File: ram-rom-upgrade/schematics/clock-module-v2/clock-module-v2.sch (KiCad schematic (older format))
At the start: 24 parts, among them SW1 SW_Push, SW2 SW_SPDT, U1 LM555, U4 74LS04, U5 74LS08, U6 74LS32

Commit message: minor tweaks
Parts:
- RV1: symbol clock-module-with-prog-halt-rescue:POT-8bit-computer-rescue-8bit-computer-rescue -> clock-module-v2-rescue:POT-8bit-computer-rescue-8bit-computer-rescue-clock-module-with-prog-halt-rescue
- SW1: symbol clock-module-with-prog-halt-rescue:SW_Push-8bit-computer-rescue-8bit-computer-rescue -> clock-module-v2-rescue:SW_Push-8bit-computer-rescue-8bit-computer-rescue-clock-module-with-prog-halt-rescue
- SW2: symbol clock-module-with-prog-halt-rescue:SW_SPDT-8bit-computer-rescue-8bit-computer-rescue -> clock-module-v2-rescue:SW_SPDT-8bit-computer-rescue-8bit-computer-rescue-clock-module-with-prog-halt-rescue
- U1: symbol clock-module-with-prog-halt-rescue:LM555-8bit-computer-rescue-8bit-computer-rescue -> clock-module-v2-rescue:LM555-8bit-computer-rescue-8bit-computer-rescue-clock-module-with-prog-halt-rescue
- U4: symbol clock-module-with-prog-halt-rescue:74LS04-8bit-computer-rescue-8bit-computer-rescue -> clock-module-v2-rescue:74LS04-8bit-computer-rescue-8bit-computer-rescue-clock-module-with-prog-halt-rescue
- U5: symbol clock-module-with-prog-halt-rescue:74LS08-8bit-computer-rescue-8bit-computer-rescue -> clock-module-v2-rescue:74LS08-8bit-computer-rescue-8bit-computer-rescue-clock-module-with-prog-halt-rescue
- U6: symbol clock-module-with-prog-halt-rescue:74LS32-8bit-computer-rescue-8bit-computer-rescue -> clock-module-v2-rescue:74LS32-8bit-computer-rescue-8bit-computer-rescue-clock-module-with-prog-halt-rescue
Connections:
- net CLK: now also U4.9; no longer U4.13
- net HLT: now also U4.11; no longer U4.9
- net PROG: now also U4.13; no longer U4.11
- net ~CLK: now also U4.8; no longer U4.12
- net at U5.12: now also U4.10; no longer U4.8
- net at U5.13: now also U4.12; no longer U4.10
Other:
- moved on the sheet: U4D, U4E, U4F
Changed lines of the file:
@@
 $EndDescr
 $Comp
-L clock-module-with-prog-halt-rescue:LM555-8bit-computer-rescue-8bit-computer-rescue U1
+L clock-module-v2-rescue:LM555-8bit-computer-rescue-8bit-computer-rescue-clock-module-with-prog-halt-rescue U1
 U 1 1 5B52B53B
 P 2000 2100
@@
 $EndComp
 $Comp
-L clock-module-with-prog-halt-rescue:POT-8bit-computer-rescue-8bit-computer-rescue RV1
+L clock-module-v2-rescue:POT-8bit-computer-rescue-8bit-computer-rescue-clock-module-with-prog-halt-rescue RV1
 U 1 1 5B52B6D7
 P 3150 2200
@@
 $EndComp
 $Comp
-L clock-module-with-prog-halt-rescue:74LS04-8bit-computer-rescue-8bit-computer-rescue U4
+L clock-module-v2-rescue:74LS04-8bit-computer-rescue-8bit-computer-rescue-clock-module-with-prog-halt-rescue U4
 U 1 1 5B52B95A
 P 3000 4900
@@
 $EndComp
 $Comp
-L clock-module-with-prog-halt-rescue:74LS08-8bit-computer-rescue-8bit-computer-rescue U5
+L clock-module-v2-rescue:74LS08-8bit-computer-rescue-8bit-computer-rescue-clock-module-with-prog-halt-rescue U5
 U 1 1 5B52B9AD
 P 4200 4200
@@
 $EndComp
 $Comp
-L clock-module-with-prog-halt-rescue:74LS32-8bit-computer-rescue-8bit-computer-rescue U6
+L clock-module-v2-rescue:74LS32-8bit-computer-rescue-8bit-computer-rescue-clock-module-with-prog-halt-rescue U6
 U 1 1 5B52B9E8
 P 5600 4600
@@
 $EndComp
 $Comp
-L clock-module-with-prog-halt-rescue:SW_SPDT-8bit-computer-rescue-8bit-computer-rescue SW2
+L clock-module-v2-rescue:SW_SPDT-8bit-computer-rescue-8bit-computer-rescue-clock-module-with-prog-halt-rescue SW2
 U 1 1 5B52BA7F
 P 6850 2200
@@
 $EndComp
 $Comp
-L clock-module-with-prog-halt-rescue:SW_Push-8bit-computer-rescue-8bit-computer-rescue SW1
+L clock-module-v2-rescue:SW_Push-8bit-computer-rescue-8bit-computer-rescue-clock-module-with-prog-halt-rescue SW1
 U 1 1 5B52BB68
 P 3950 1900
@@
 NoConn ~ 8450 2100
 $Comp
-L clock-module-with-prog-halt-rescue:74LS08-8bit-computer-rescue-8bit-computer-rescue U5
+L clock-module-v2-rescue:74LS08-8bit-computer-rescue-8bit-computer-rescue-clock-module-with-prog-halt-rescue U5
 U 2 1 5B52E719
 P 4200 5000
@@
 $EndComp
 $Comp
-L clock-module-with-prog-halt-rescue:74LS08-8bit-computer-rescue-8bit-computer-rescue U5
+L clock-module-v2-rescue:74LS08-8bit-computer-rescue-8bit-computer-rescue-clock-module-with-prog-halt-rescue U5
 U 3 1 5B52E764
 P 7000 4700
@@
 $EndComp
 $Comp
-L clock-module-with-prog-halt-rescue:74LS04-8bit-computer-rescue-8bit-computer-rescue U4
+L clock-module-v2-rescue:74LS04-8bit-computer-rescue-8bit-computer-rescue-clock-module-with-prog-halt-rescue U4
 U 4 1 5B52E7BF
-P 3000 5800
-F 0 "U4" H 3195 5915 50  0000 C CNN
-F 1 "74LS04" H 3190 5675 50  0000 C CNN
-F 2 "Package_DIP:DIP-14_W7.62mm" H 3000 5800 50  0001 C CNN
-F 3 "" H 3000 5800 50  0001 C CNN
-	4    3000 5800
-	1    0    0    -1
-$EndComp
-$Comp
-L clock-module-with-prog-halt-rescue:74LS04-8bit-computer-rescue-8bit-computer-rescue U4
-U 6 1 5B52E82B
 P 8800 4250
 F 0 "U4" H 8995 4365 50  0000 C CNN
@@
 F 2 "Package_DIP:DIP-14_W7.62mm" H 8800 4250 50  0001 C CNN
 F 3 "" H 8800 4250 50  0001 C CNN
-	6    8800 4250
+	4    8800 4250
+	1    0    0    -1
+$EndComp
+$Comp
+L clock-module-v2-rescue:74LS04-8bit-computer-rescue-8bit-computer-rescue-clock-module-with-prog-halt-rescue U4
+U 6 1 5B52E82B
+P 2250 6000
+F 0 "U4" H 2445 6115 50  0000 C CNN
+F 1 "74LS04" H 2440 5875 50  0000 C CNN
+F 2 "Package_DIP:DIP-14_W7.62mm" H 2250 6000 50  0001 C CNN
+F 3 "" H 2250 6000 50  0001 C CNN
+	6    2250 6000
 	1    0    0    -1
 $EndComp
@@
 	9900 1750 9900 1850
 $Comp
-L clock-module-with-prog-halt-rescue:74LS04-8bit-computer-rescue-8bit-computer-rescue U4
+L clock-module-v2-rescue:74LS04-8bit-computer-rescue-8bit-computer-rescue-clock-module-with-prog-halt-rescue U4
 U 2 1 5B5304B0
 P 1700 6650
@@
 $EndComp
 $Comp
-L clock-module-with-prog-halt-rescue:74LS04-8bit-computer-rescue-8bit-computer-rescue U4
+L clock-module-v2-rescue:74LS04-8bit-computer-rescue-8bit-computer-rescue-clock-module-with-prog-halt-rescue U4
 U 3 1 5B5304FB
 P 1700 7050
@@
 $EndComp
 $Comp
-L clock-module-with-prog-halt-rescue:74LS04-8bit-computer-rescue-8bit-computer-rescue U4
+L clock-module-v2-rescue:74LS04-8bit-computer-rescue-8bit-computer-rescue-clock-module-with-prog-halt-rescue U4
 U 5 1 5B53108F
-P 2250 6000
-F 0 "U4" H 2445 6115 50  0000 C CNN
-F 1 "74LS04" H 2440 5875 50  0000 C CNN
-F 2 "Package_DIP:DIP-14_W7.62mm" H 2250 6000 50  0001 C CNN
-F 3 "" H 2250 6000 50  0001 C CNN
-	5    2250 6000
-	1    0    0    -1
-$EndComp
-$Comp
-L clock-module-with-prog-halt-rescue:74LS08-8bit-computer-rescue-8bit-computer-rescue U5
+P 3000 5800
+F 0 "U4" H 3195 5915 50  0000 C CNN
+F 1 "74LS04" H 3190 5675 50  0000 C CNN
+F 2 "Package_DIP:DIP-14_W7.62mm" H 3000 5800 50  0001 C CNN
+F 3 "" H 3000 5800 50  0001 C CNN
+	5    3000 5800
+	1    0    0    -1
+$EndComp
+$Comp
+L clock-module-v2-rescue:74LS08-8bit-computer-rescue-8bit-computer-rescue-clock-module-with-prog-halt-rescue U5
 U 4 1 5B53125C
 P 4250 5900
@@
 $EndComp
 $Comp
-L clock-module-with-prog-halt-rescue:74LS32-8bit-computer-rescue-8bit-computer-rescue U6
+L clock-module-v2-rescue:74LS32-8bit-computer-rescue-8bit-computer-rescue-clock-module-with-prog-halt-rescue U6
 U 2 1 5B5312F6
 P 3000 7400
@@
 $EndComp
 $Comp
-L clock-module-with-prog-halt-rescue:74LS32-8bit-computer-rescue-8bit-computer-rescue U6
+L clock-module-v2-rescue:74LS32-8bit-computer-rescue-8bit-computer-rescue-clock-module-with-prog-halt-rescue U6
 U 3 1 5B5313CF
 P 4350 6800
@@
 PROG
 $Comp
-L clock-module-with-prog-halt-rescue:74LS32-8bit-computer-rescue-8bit-computer-rescue U6
+L clock-module-v2-rescue:74LS32-8bit-computer-rescue-8bit-computer-rescue-clock-module-with-prog-halt-rescue U6
 U 4 1 5B531491
 P 4350 7400

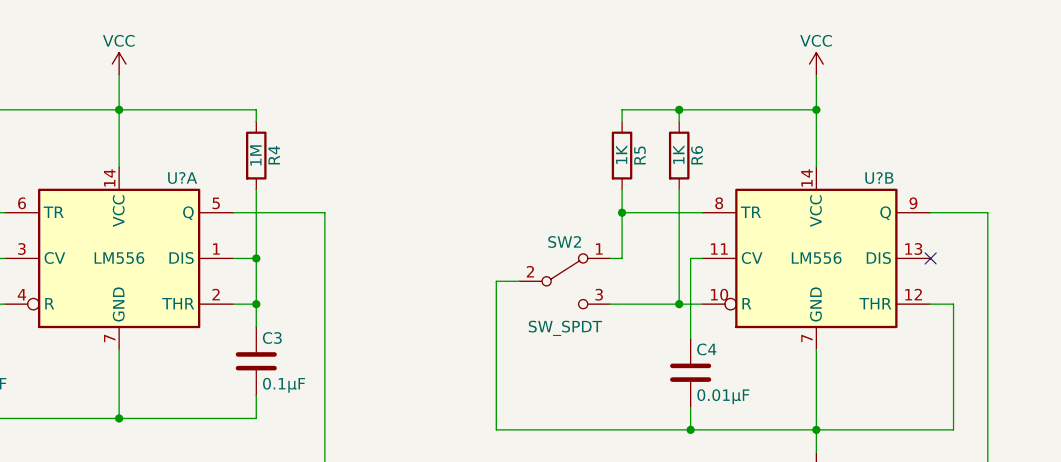
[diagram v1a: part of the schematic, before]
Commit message: added annotations
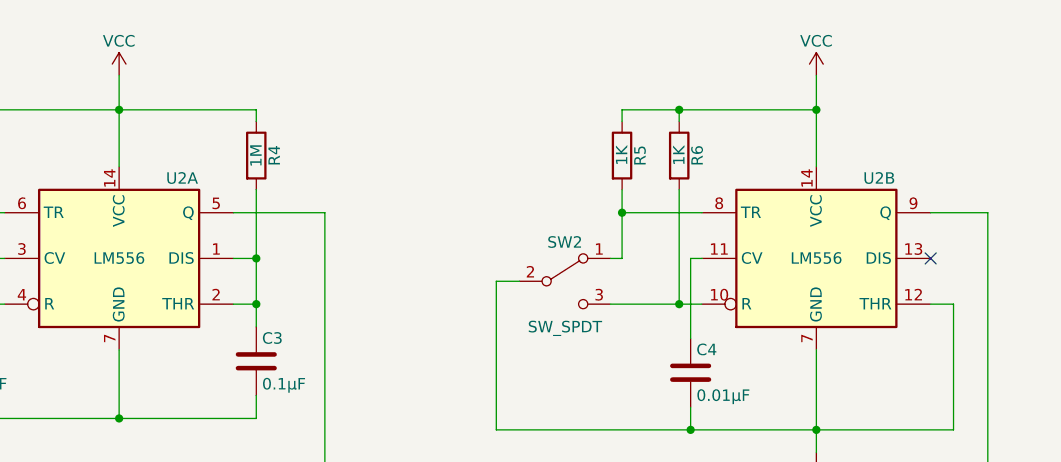
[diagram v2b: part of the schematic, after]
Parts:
- gave numbers to parts that had none: 1
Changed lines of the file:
@@
 	2700 6000 3650 6000
 $Comp
-L Timer:LM556 U?
+L Timer:LM556 U2
 U 1 1 607D2826
 P 4900 2100
-F 0 "U?" H 5175 2450 50  0000 C CNN
+F 0 "U2" H 5175 2450 50  0000 C CNN
 F 1 "LM556" H 4900 2100 50  0000 C CNN
 F 2 "" H 4900 2100 50  0001 C CNN
@@
 $EndComp
 $Comp
-L Timer:LM556 U?
+L Timer:LM556 U2
 U 2 1 607D78F1
 P 7950 2100
-F 0 "U?" H 8225 2450 50  0000 C CNN
+F 0 "U2" H 8225 2450 50  0000 C CNN
 F 1 "LM556" H 7950 2100 50  0000 C CNN
 F 2 "" H 7950 2100 50  0001 C CNN

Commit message: candidate final schematic designs
Also started to consolidate custom symbols from all projects
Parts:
- RV1: symbol clock-module-v2-rescue:POT-8bit-computer-rescue-8bit-computer-rescue-clock-module-with-prog-halt-rescue -> Device:R_POT
- SW1: symbol clock-module-v2-rescue:SW_Push-8bit-computer-rescue-8bit-computer-rescue-clock-module-with-prog-halt-rescue -> Switch:SW_Push
- SW2: symbol clock-module-v2-rescue:SW_SPDT-8bit-computer-rescue-8bit-computer-rescue-clock-module-with-prog-halt-rescue -> Switch:SW_SPDT
- U1: symbol clock-module-v2-rescue:LM555-8bit-computer-rescue-8bit-computer-rescue-clock-module-with-prog-halt-rescue -> Timer:LM555xN
- U4: symbol clock-module-v2-rescue:74LS04-8bit-computer-rescue-8bit-computer-rescue-clock-module-with-prog-halt-rescue -> 74xx:74LS04
- U5: symbol clock-module-v2-rescue:74LS08-8bit-computer-rescue-8bit-computer-rescue-clock-module-with-prog-halt-rescue -> 74xx:74LS08
- U6: symbol clock-module-v2-rescue:74LS32-8bit-computer-rescue-8bit-computer-rescue-clock-module-with-prog-halt-rescue -> 74xx:74LS32
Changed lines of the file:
@@
 $EndDescr
 $Comp
-L clock-module-v2-rescue:LM555-8bit-computer-rescue-8bit-computer-rescue-clock-module-with-prog-halt-rescue U1
+L Timer:LM555xN U1
 U 1 1 5B52B53B
 P 2000 2100
@@
 $EndComp
 $Comp
-L clock-module-v2-rescue:POT-8bit-computer-rescue-8bit-computer-rescue-clock-module-with-prog-halt-rescue RV1
+L Device:R_POT RV1
 U 1 1 5B52B6D7
 P 3150 2200
@@
 $EndComp
 $Comp
-L clock-module-v2-rescue:74LS04-8bit-computer-rescue-8bit-computer-rescue-clock-module-with-prog-halt-rescue U4
+L 74xx:74LS04 U4
 U 1 1 5B52B95A
 P 3000 4900
@@
 $EndComp
 $Comp
-L clock-module-v2-rescue:74LS08-8bit-computer-rescue-8bit-computer-rescue-clock-module-with-prog-halt-rescue U5
+L 74xx:74LS08 U5
 U 1 1 5B52B9AD
 P 4200 4200
@@
 $EndComp
 $Comp
-L clock-module-v2-rescue:74LS32-8bit-computer-rescue-8bit-computer-rescue-clock-module-with-prog-halt-rescue U6
+L 74xx:74LS32 U6
 U 1 1 5B52B9E8
 P 5600 4600
@@
 $EndComp
 $Comp
-L clock-module-v2-rescue:SW_SPDT-8bit-computer-rescue-8bit-computer-rescue-clock-module-with-prog-halt-rescue SW2
+L Switch:SW_SPDT SW2
 U 1 1 5B52BA7F
 P 6850 2200
@@
 $EndComp
 $Comp
-L clock-module-v2-rescue:SW_Push-8bit-computer-rescue-8bit-computer-rescue-clock-module-with-prog-halt-rescue SW1
+L Switch:SW_Push SW1
 U 1 1 5B52BB68
 P 3950 1900
@@
 NoConn ~ 8450 2100
 $Comp
-L clock-module-v2-rescue:74LS08-8bit-computer-rescue-8bit-computer-rescue-clock-module-with-prog-halt-rescue U5
+L 74xx:74LS08 U5
 U 2 1 5B52E719
 P 4200 5000
@@
 $EndComp
 $Comp
-L clock-module-v2-rescue:74LS08-8bit-computer-rescue-8bit-computer-rescue-clock-module-with-prog-halt-rescue U5
+L 74xx:74LS08 U5
 U 3 1 5B52E764
 P 7000 4700
@@
 $EndComp
 $Comp
-L clock-module-v2-rescue:74LS04-8bit-computer-rescue-8bit-computer-rescue-clock-module-with-prog-halt-rescue U4
+L 74xx:74LS04 U4
 U 4 1 5B52E7BF
 P 8800 4250
@@
 $EndComp
 $Comp
-L clock-module-v2-rescue:74LS04-8bit-computer-rescue-8bit-computer-rescue-clock-module-with-prog-halt-rescue U4
+L 74xx:74LS04 U4
 U 6 1 5B52E82B
 P 2250 6000
@@
 $EndComp
 Wire Wire Line
-	3450 4900 3600 4900
-Wire Wire Line
-	4800 4200 4900 4200
-Wire Wire Line
 	4900 4200 4900 4500
 Wire Wire Line
-	4900 4500 5000 4500
-Wire Wire Line
-	5000 4700 4900 4700
-Wire Wire Line
 	4900 4700 4900 5000
 Wire Wire Line
-	4900 5000 4800 5000
-Wire Wire Line
-	6200 4600 6400 4600
-Wire Wire Line
-	6300 4800 6400 4800
-Wire Wire Line
-	2400 4900 2550 4900
-Wire Wire Line
 	2400 3700 2400 4300
 Wire Wire Line
-	2400 4300 3600 4300
-Wire Wire Line
 	2500 1900 3450 1900
 Wire Wire Line
-	3450 4100 3600 4100
-Wire Wire Line
 	5400 1900 5800 1900
 Wire Wire Line
@@
 Wire Wire Line
 	2150 3550 2150 5100
-Wire Wire Line
-	2150 5100 3600 5100
 Wire Wire Line
 	3450 1900 3450 4100
@@
 Text HLabel 1450 5800 0    60   Input ~ 0
 HLT
-Wire Wire Line
-	1450 5800 2550 5800
 Wire Wire Line
 	7900 5200 7900 5350
@@
 ~CLK
 Wire Wire Line
-	9700 4250 9250 4250
-Wire Wire Line
-	7600 4700 7900 4700
-Wire Wire Line
 	7900 4250 7900 4700
 Connection ~ 7900 4700
-Wire Wire Line
-	7900 4250 8350 4250
 $Comp
 L Device:C C1
@@
 	9900 1750 9900 1850
 $Comp
-L clock-module-v2-rescue:74LS04-8bit-computer-rescue-8bit-computer-rescue-clock-module-with-prog-halt-rescue U4
+L 74xx:74LS04 U4
 U 2 1 5B5304B0
 P 1700 6650
@@
 $EndComp
 $Comp
-L clock-module-v2-rescue:74LS04-8bit-computer-rescue-8bit-computer-rescue-clock-module-with-prog-halt-rescue U4
+L 74xx:74LS04 U4
 U 3 1 5B5304FB
 P 1700 7050
@@
 $EndComp
 $Comp
-L clock-module-v2-rescue:74LS04-8bit-computer-rescue-8bit-computer-rescue-clock-module-with-prog-halt-rescue U4
+L 74xx:74LS04 U4
 U 5 1 5B53108F
 P 3000 5800
@@
 $EndComp
 $Comp
-L clock-module-v2-rescue:74LS08-8bit-computer-rescue-8bit-computer-rescue-clock-module-with-prog-halt-rescue U5
+L 74xx:74LS08 U5
 U 4 1 5B53125C
 P 4250 5900
@@
 $EndComp
 $Comp
-L clock-module-v2-rescue:74LS32-8bit-computer-rescue-8bit-computer-rescue-clock-module-with-prog-halt-rescue U6
+L 74xx:74LS32 U6
 U 2 1 5B5312F6
 P 3000 7400
@@
 $EndComp
 $Comp
-L clock-module-v2-rescue:74LS32-8bit-computer-rescue-8bit-computer-rescue-clock-module-with-prog-halt-rescue U6
+L 74xx:74LS32 U6
 U 3 1 5B5313CF
 P 4350 6800
@@
 	1    0    0    -1
 $EndComp
-NoConn ~ 2150 6650
-NoConn ~ 1250 6650
-NoConn ~ 1250 7050
-NoConn ~ 2150 7050
-NoConn ~ 3600 7400
-NoConn ~ 2400 7300
-NoConn ~ 2400 7500
-NoConn ~ 3750 6700
-NoConn ~ 3750 6900
-NoConn ~ 4950 6800
+NoConn ~ 2000 6650
+NoConn ~ 1400 6650
+NoConn ~ 1400 7050
+NoConn ~ 2000 7050
+NoConn ~ 3300 7400
+NoConn ~ 2700 7300
+NoConn ~ 2700 7500
+NoConn ~ 4050 6700
+NoConn ~ 4050 6900
+NoConn ~ 4650 6800
 Wire Wire Line
 	7950 2500 7950 2850
@@
 Wire Wire Line
 	9750 1850 9900 1850
-NoConn ~ 3750 7500
-NoConn ~ 3750 7300
-NoConn ~ 4950 7400
+NoConn ~ 4050 7500
+NoConn ~ 4050 7300
+NoConn ~ 4650 7400
 Text HLabel 1450 6000 0    50   Input ~ 0
 PROG
 $Comp
-L clock-module-v2-rescue:74LS32-8bit-computer-rescue-8bit-computer-rescue-clock-module-with-prog-halt-rescue U6
+L 74xx:74LS32 U6
 U 4 1 5B531491
 P 4350 7400
@@
 $EndComp
 Wire Wire Line
-	3450 5800 3650 5800
-Wire Wire Line
-	4850 5900 6300 5900
-Wire Wire Line
 	6300 4800 6300 5900
-Wire Wire Line
-	1450 6000 1800 6000
-Wire Wire Line
-	2700 6000 3650 6000
 $Comp
 L Timer:LM556 U2
@@
 	1    0    0    -1
 $EndComp
+Wire Wire Line
+	4500 4200 4900 4200
+Wire Wire Line
+	4500 5000 4900 5000
+Wire Wire Line
+	3450 4100 3900 4100
+Wire Wire Line
+	2400 4300 3900 4300
+Wire Wire Line
+	2150 5100 3900 5100
+Wire Wire Line
+	6300 4800 6700 4800
+Wire Wire Line
+	4550 5900 6300 5900
+Wire Wire Line
+	3300 5800 3950 5800
+Wire Wire Line
+	3300 4900 3900 4900
+Wire Wire Line
+	2400 4900 2700 4900
+Wire Wire Line
+	1450 5800 2700 5800
+Wire Wire Line
+	1450 6000 1950 6000
+Wire Wire Line
+	2550 6000 3950 6000
+Wire Wire Line
+	9100 4250 9700 4250
+Wire Wire Line
+	7900 4250 8500 4250
+Wire Wire Line
+	7300 4700 7900 4700
+Wire Wire Line
+	5900 4600 6700 4600
+Wire Wire Line
+	4900 4500 5300 4500
+Wire Wire Line
+	4900 4700 5300 4700
 $EndSCHEMATC
